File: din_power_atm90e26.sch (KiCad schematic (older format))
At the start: 62 parts, among them J1 CONN_01X06, J2 VBAT, J3 CONN_01X08, J4 CONN_02X18, J5 CONN_01X08, U1 MCP73831-2-OT, U2 AP7365-33YG-13, U3 AP7365-33YG-13, U4 Hi-Link_SMPS, U5 dc-dc

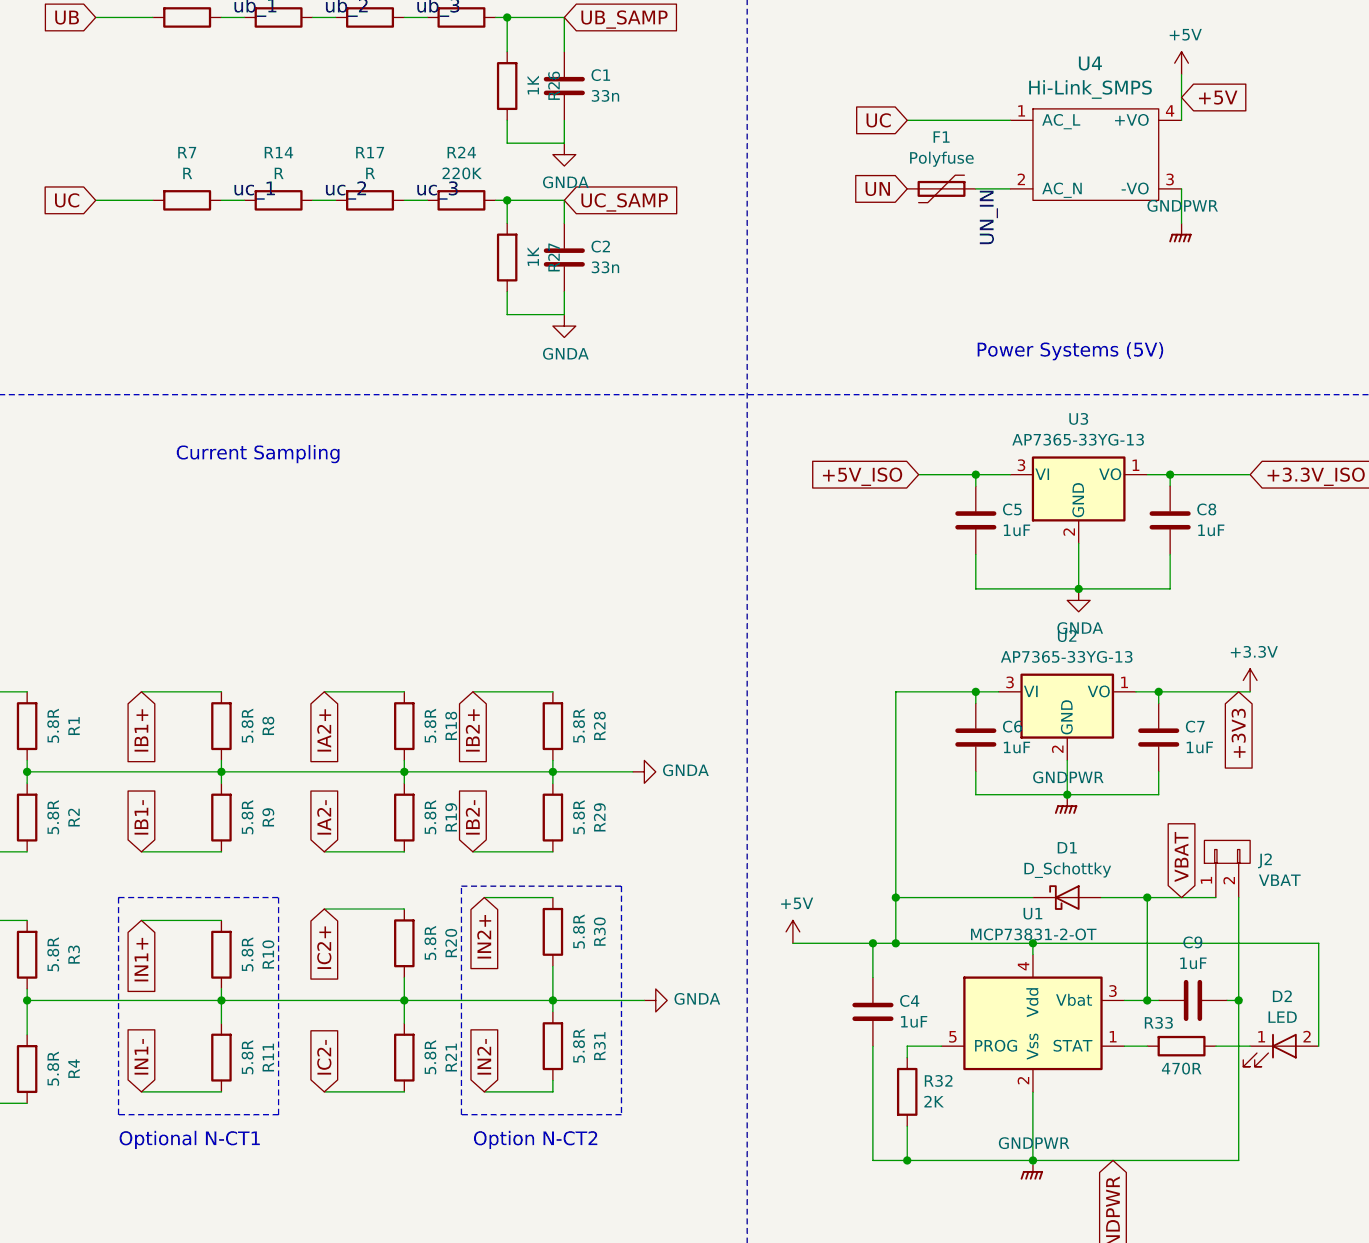
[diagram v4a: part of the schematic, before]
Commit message: Update parts to fit Kicost
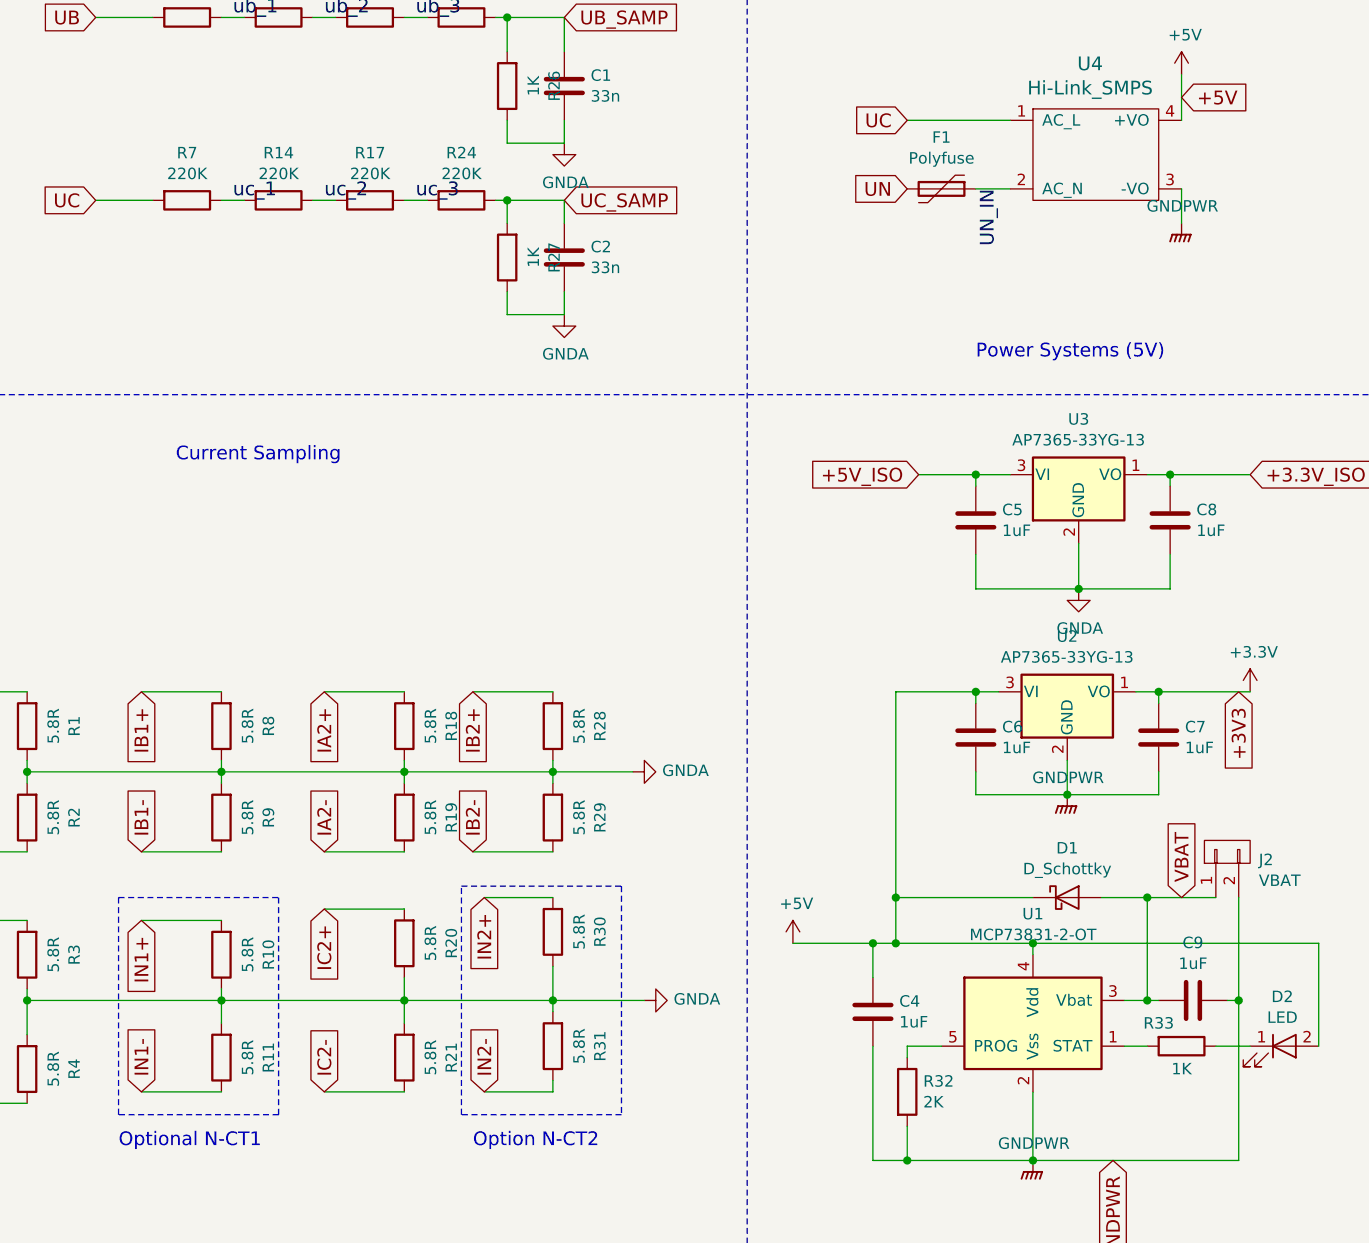
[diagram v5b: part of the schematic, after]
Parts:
- C3: manf# (none) -> CC0603KRX7R9BB333
- D2: manf# (none) -> LTST-C190KRKT
- G1, LOGO_OSHW1, SYM1: DNP (none) -> 1
- J1: manf# (none) -> 1759059
- J2: manf# (none) -> BM02B-SRSS-TB(LFSN)
- J3, J5: manf# (none) -> 1053141108
- J4: manf# (none) -> 10018784-10210TLF
- L1: manf# (none) -> AIML-1206-R27K-T
- R14, R17, R7: value R -> 220K
- R32: manf# (none) -> RT0603DRE072KL
- R33: value 470R -> 1K
- U4: kicost:pricing (none) -> 50:$2.74
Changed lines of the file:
@@
 F 2 "hi-link_smps:HKLPM01" H 850 -400 60  0001 C CNN
 F 3 "" H 850 -400 60  0001 C CNN
+F 4 "50:$2.74" H 5600 2900 60  0001 C CNN "kicost:pricing"
 	1    5600 2900
 	1    0    0    -1
@@
 F 2 "hi-link_smps:PCIE-36-SKT" H 5250 800 50  0001 C CNN
 F 3 "" H 5250 800 50  0001 C CNN
+F 4 "10018784-10210TLF" H 9050 5200 60  0001 C CNN "manf#"
 	1    9050 5200
 	0    1    1    0
@@
 F 2 "Connectors_Molex:Molex_NanoFit_2x04x2.50mm_Angled" H 5850 -3600 50  0001 C CNN
 F 3 "" H 5850 -3600 50  0001 C CNN
+F 4 "1053141108" H 9700 1350 60  0001 C CNN "manf#"
 	1    9700 1350
 	0    -1   -1   0
@@
 F 2 "Connectors_Molex:Molex_NanoFit_2x04x2.50mm_Angled" H 4700 -3600 50  0001 C CNN
 F 3 "" H 4700 -3600 50  0001 C CNN
+F 4 "1053141108" H 8550 1350 60  0001 C CNN "manf#"
 	1    8550 1350
 	0    -1   -1   0
@@
 F 2 "Connectors_Phoenix:PhoenixContact_MC-G_06x5.08mm_Angled" H 3150 -350 50  0001 C CNN
 F 3 "" H 3150 -350 50  0001 C CNN
+F 4 "1759059" H 4350 1150 60  0001 C CNN "manf#"
 	1    4350 1150
 	-1   0    0    -1
@@
 P 1650 2850
 F 0 "R7" V 1443 2850 50  0000 C CNN
-F 1 "R" V 1534 2850 50  0000 C CNN
+F 1 "220K" V 1534 2850 50  0000 C CNN
 F 2 "Resistors_SMD:R_1206" V 1580 2850 50  0001 C CNN
 F 3 "" H 1650 2850 50  0001 C CNN
@@
 P 2050 2850
 F 0 "R14" V 1843 2850 50  0000 C CNN
-F 1 "R" V 1934 2850 50  0000 C CNN
+F 1 "220K" V 1934 2850 50  0000 C CNN
 F 2 "Resistors_SMD:R_1206" V 1980 2850 50  0001 C CNN
 F 3 "" H 2050 2850 50  0001 C CNN
@@
 P 2450 2850
 F 0 "R17" V 2243 2850 50  0000 C CNN
-F 1 "R" V 2334 2850 50  0000 C CNN
+F 1 "220K" V 2334 2850 50  0000 C CNN
 F 2 "Resistors_SMD:R_1206" V 2380 2850 50  0001 C CNN
 F 3 "" H 2450 2850 50  0001 C CNN
@@
 F 2 "Capacitors_SMD:C_0603" H 3388 1150 50  0001 C CNN
 F 3 "" H 3350 1300 50  0001 C CNN
+F 4 "CC0603KRX7R9BB333" H 3350 1300 60  0001 C CNN "manf#"
 	1    3350 1300
 	1    0    0    -1
@@
 F 2 "Inductors_SMD:L_1206" V 4730 1550 50  0001 C CNN
 F 3 "" H 4800 1550 50  0001 C CNN
+F 4 "AIML-1206-R27K-T" H 4800 1550 60  0001 C CNN "manf#"
 	1    4800 1550
 	0    1    1    0
@@
 F 2 "Connectors_JST:JST_SH_BM02B-SRSS-TB_02x1.00mm_Straight" H 6200 5700 50  0001 C CNN
 F 3 "" H 6200 5700 50  0001 C CNN
+F 4 "BM02B-SRSS-TB(LFSN)" H 6200 5700 60  0001 C CNN "manf#"
 	1    6200 5700
 	0    -1   -1   0
@@
 F 2 "Resistors_SMD:R_0603" V 4730 6750 50  0001 C CNN
 F 3 "" H 4800 6750 50  0001 C CNN
+F 4 "RT0603DRE072KL" H 4800 6750 60  0001 C CNN "manf#"
 	1    4800 6750
 	1    0    0    -1
@@
 P 6000 6550
 F 0 "R33" V 5900 6450 50  0000 C CNN
-F 1 "470R" V 6100 6550 50  0000 C CNN
+F 1 "1K" V 6100 6550 50  0000 C CNN
 F 2 "Resistors_SMD:R_0603" V 5930 6550 50  0001 C CNN
 F 3 "" H 6000 6550 50  0001 C CNN
@@
 F 2 "LEDs:LED_0603" H 6450 6550 50  0001 C CNN
 F 3 "" H 6450 6550 50  0001 C CNN
+F 4 "LTST-C190KRKT" H 6450 6550 60  0001 C CNN "manf#"
 	1    6450 6550
 	1    0    0    -1
@@
 F 2 "Whatnick_logo:Fsilk_HV" H 8250 2575 50  0001 C CNN
 F 3 "" H 8650 2500 50  0001 C CNN
+F 4 "1" V 8250 2600 60  0001 C CNN "DNP"
 	1    8250 2600
 	1    0    0    -1
@@
 F 2 "Whatnick_logo:Whatnick_logo" H 9000 2600 60  0001 C CNN
 F 3 "" H 9000 2600 60  0001 C CNN
+F 4 "1" H 9000 2600 60  0001 C CNN "DNP"
 	1    9000 2600
 	1    0    0    -1
@@
 F 2 "Symbols:OSHW-Symbol_6.7x6mm_SilkScreen" H 9850 2600 50  0001 C CNN
 F 3 "" H 9850 2600 50  0001 C CNN
+F 4 "1" H 9850 2600 60  0001 C CNN "DNP"
 	1    9850 2600
 	1    0    0    -1
